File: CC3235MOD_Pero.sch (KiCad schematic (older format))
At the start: 38 parts, among them J1 USB_B_Mini, J2 JTAG/SWD, SW1 Reset, SW2 SW_DIP_x03, SW3 User IO, U1 TLV1117-33, U2 CP2102N-A01-GQFN24, U3 CC3235MODSF12MOBR

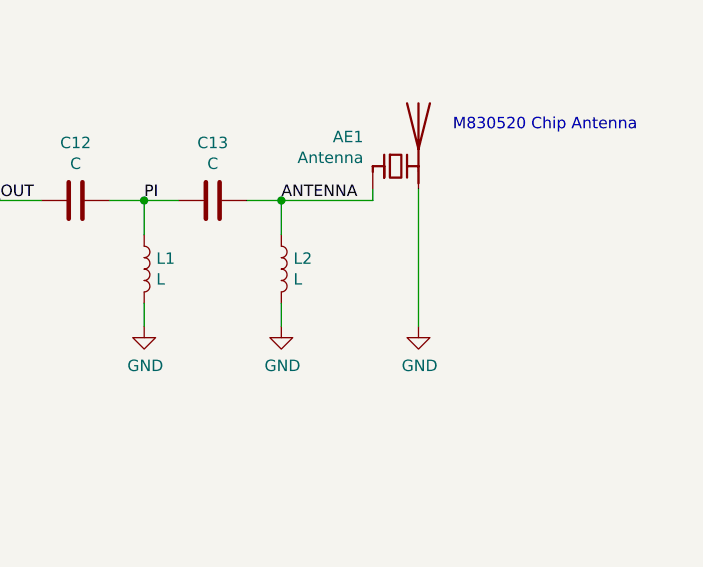
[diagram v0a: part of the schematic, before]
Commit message: fixint antenna footprint
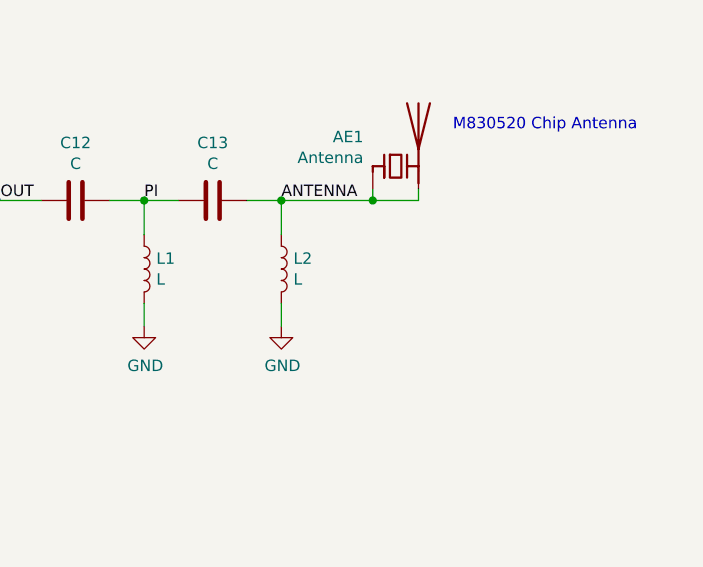
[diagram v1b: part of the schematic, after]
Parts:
- C12, C13: footprint Capacitors_SMD:C_0402 -> Capacitor_SMD:C_0603_1608Metric
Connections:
- net ANTENNA: now also AE1.2 (PCB_Trace)
- net GND: no longer AE1.2 (PCB_Trace)
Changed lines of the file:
@@
 F 0 "C12" V 12448 6700 50  0000 C CNN
 F 1 "C" V 12539 6700 50  0000 C CNN
-F 2 "Capacitors_SMD:C_0402" H 12738 6550 50  0001 C CNN
+F 2 "Capacitor_SMD:C_0603_1608Metric" H 12738 6550 50  0001 C CNN
 F 3 "~" H 12700 6700 50  0001 C CNN
 	1    12700 6700
@@
 F 0 "C13" V 13048 6700 50  0000 C CNN
 F 1 "C" V 13139 6700 50  0000 C CNN
-F 2 "Capacitors_SMD:C_0402" H 13338 6550 50  0001 C CNN
+F 2 "Capacitor_SMD:C_0603_1608Metric" H 13338 6550 50  0001 C CNN
 F 3 "~" H 13300 6700 50  0001 C CNN
 	1    13300 6700
@@
 	14000 6650 14000 6700
 Wire Wire Line
-	14200 6650 14200 7250
-$Comp
-L power:GND #PWR040
-U 1 1 5EE1CAB8
-P 14200 7250
-F 0 "#PWR040" H 14200 7000 50  0001 C CNN
-F 1 "GND" H 14205 7077 50  0000 C CNN
-F 2 "" H 14200 7250 50  0001 C CNN
-F 3 "" H 14200 7250 50  0001 C CNN
-	1    14200 7250
-	1    0    0    -1
-$EndComp
+	14200 6650 14200 6700
 NoConn ~ 11450 3250
 NoConn ~ 11450 3350
@@
 Text Label 13600 6700 0    50   ~ 0
 ANTENNA
+Wire Wire Line
+	14000 6700 14200 6700
+Connection ~ 14000 6700
 $EndSCHEMATC

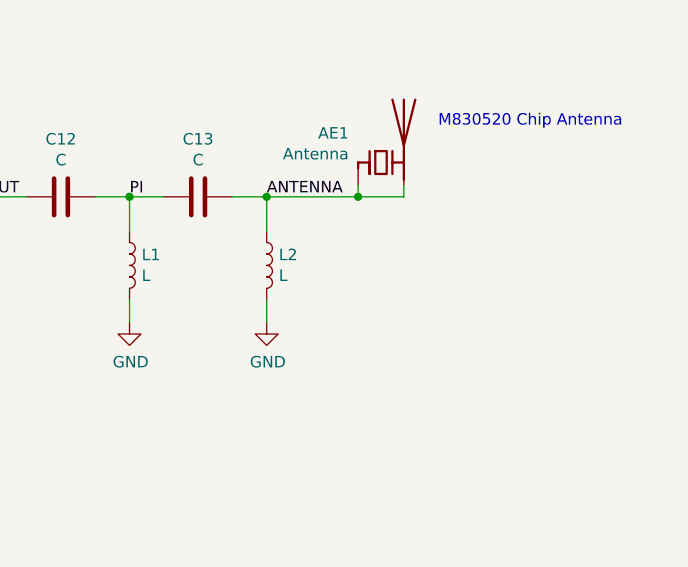
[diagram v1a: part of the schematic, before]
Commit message: antenna gnd solved
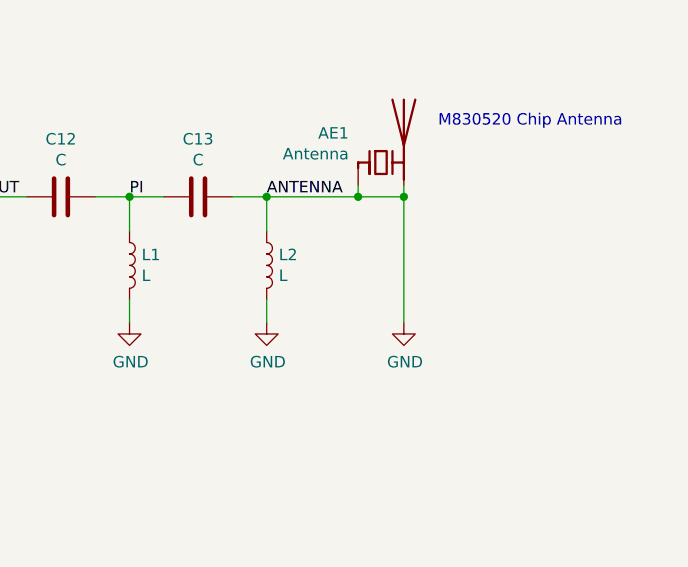
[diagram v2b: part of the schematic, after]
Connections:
- net ANTENNA is gone; now on net GND: AE1.1 (FEED), AE1.2 (PCB_Trace), C13.1, L2.1
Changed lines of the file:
@@
 	14000 6700 14200 6700
 Connection ~ 14000 6700
+$Comp
+L power:GND #PWR?
+U 1 1 5EF1A7C2
+P 14200 7250
+F 0 "#PWR?" H 14200 7000 50  0001 C CNN
+F 1 "GND" H 14205 7077 50  0000 C CNN
+F 2 "" H 14200 7250 50  0001 C CNN
+F 3 "" H 14200 7250 50  0001 C CNN
+	1    14200 7250
+	1    0    0    -1
+$EndComp
+Wire Wire Line
+	14200 7250 14200 6700
+Connection ~ 14200 6700
 $EndSCHEMATC

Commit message: fixed footprint associations AGAIN!
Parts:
- C1, C2: footprint Capacitors_SMD:C_0805 -> Capacitor_SMD:C_0805_2012Metric
- C10, C11, C3, C4, C5, C6, C7, C8, C9: footprint Capacitors_SMD:C_0603 -> Capacitor_SMD:C_0603_1608Metric
- D1: footprint TO_SOT_Packages_SMD:SOT-143 -> Package_TO_SOT_SMD:SOT-143R_Reverse; symbol CC3235MOD_Pero-rescue:SP0503BAHT-Power_Protection -> CC3235MOD_Pero-rescue:SP0503BAHT-Power_Protection-CC3235MOD_Pero-rescue
- D2, D3, D4: footprint LEDs:LED_0603 -> LED_SMD:LED_0603_1608Metric
- F1: footprint Fuse_Holders_and_Fuses:Fuse_SMD1206_Reflow -> Fuse:Fuse_1206_3216Metric
- J1: footprint Connectors_USB:USB_Micro-B_Molex-105017-0001 -> Connector_USB:USB_Micro-AB_Molex_47590-0001
- J2: footprint Pin_Headers:Pin_Header_Straight_2x05_Pitch2.54mm -> Connector_PinHeader_2.54mm:PinHeader_2x05_P2.54mm_Vertical; symbol CC3235MOD_Pero-rescue:Conn_ARM_JTAG_SWD_10-Connector -> CC3235MOD_Pero-rescue:Conn_ARM_JTAG_SWD_10-Connector-CC3235MOD_Pero-rescue
- L1, L2: footprint Inductors_SMD:L_0603 -> Inductor_SMD:L_0603_1608Metric
- R1, R2, R3, R4, R5, R6, R7, R8, R9: footprint Resistors_SMD:R_0603 -> Resistor_SMD:R_0603_1608Metric
- SW1, SW3: footprint Buttons_Switches_SMD:SW_SPST_EVQP0 -> Button_Switch_SMD:SW_SPST_EVQP0
- SW2: footprint Buttons_Switches_SMD:SW_DIP_x3_W8.61mm_Slide_LowProfile -> Button_Switch_SMD:SW_DIP_SPSTx03_Slide_6.7x9.18mm_W8.61mm_P2.54mm_LowProfile
- U1: footprint TO_SOT_Packages_SMD:SOT-223-3_TabPin2 -> Package_TO_SOT_SMD:SOT-223-3_TabPin2
- U2: footprint Housings_DFN_QFN:QFN-24-1EP_4x4mm_Pitch0.5mm -> Package_DFN_QFN:HVQFN-24-1EP_4x4mm_P0.5mm_EP2.5x2.5mm
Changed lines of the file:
@@
 $EndDescr
 $Comp
-L CC3235MOD_Pero-rescue:Conn_ARM_JTAG_SWD_10-Connector J2
+L CC3235MOD_Pero-rescue:Conn_ARM_JTAG_SWD_10-Connector-CC3235MOD_Pero-rescue J2
 U 1 1 5EC52D94
 P 6600 4450
 F 0 "J2" H 6250 5150 50  0000 R CNN
 F 1 "JTAG/SWD" H 6500 5050 50  0000 R CNN
-F 2 "Pin_Headers:Pin_Header_Straight_2x05_Pitch2.54mm" H 6650 3900 50  0001 L TNN
+F 2 "Connector_PinHeader_2.54mm:PinHeader_2x05_P2.54mm_Vertical" H 6650 3900 50  0001 L TNN
 F 3 "http://infocenter.arm.com/help/topic/com.arm.doc.faqs/attached/13634/cortex_debug_connectors.pdf" V 6250 3200 50  0001 C CNN
 	1    6600 4450
@@
 F 0 "R5" H 8300 3000 50  0000 L CNN
 F 1 "DNI(10K)" H 8050 2900 50  0000 L CNN
-F 2 "Resistors_SMD:R_0603" V 8380 2950 50  0001 C CNN
+F 2 "Resistor_SMD:R_0603_1608Metric" V 8380 2950 50  0001 C CNN
 F 3 "~" H 8450 2950 50  0001 C CNN
 	1    8450 2950
@@
 F 0 "R6" H 8820 2996 50  0000 L CNN
 F 1 "DNI" H 8820 2905 50  0000 L CNN
-F 2 "Resistors_SMD:R_0603" V 8680 2950 50  0001 C CNN
+F 2 "Resistor_SMD:R_0603_1608Metric" V 8680 2950 50  0001 C CNN
 F 3 "~" H 8750 2950 50  0001 C CNN
 	1    8750 2950
@@
 F 0 "L1" H 13053 7046 50  0000 L CNN
 F 1 "L" H 13053 6955 50  0000 L CNN
-F 2 "Inductors_SMD:L_0603" H 13000 7000 50  0001 C CNN
+F 2 "Inductor_SMD:L_0603_1608Metric" H 13000 7000 50  0001 C CNN
 F 3 "~" H 13000 7000 50  0001 C CNN
 	1    13000 7000
@@
 F 0 "L2" H 13653 7046 50  0000 L CNN
 F 1 "L" H 13653 6955 50  0000 L CNN
-F 2 "Inductors_SMD:L_0603" H 13600 7000 50  0001 C CNN
+F 2 "Inductor_SMD:L_0603_1608Metric" H 13600 7000 50  0001 C CNN
 F 3 "~" H 13600 7000 50  0001 C CNN
 	1    13600 7000
@@
 F 0 "SW1" H 8100 3735 50  0000 C CNN
 F 1 "Reset" H 8100 3644 50  0000 C CNN
-F 2 "Buttons_Switches_SMD:SW_SPST_EVQP0" H 8100 3650 50  0001 C CNN
+F 2 "Button_Switch_SMD:SW_SPST_EVQP0" H 8100 3650 50  0001 C CNN
 F 3 "" H 8100 3650 50  0001 C CNN
 	1    8100 3450
@@
 F 0 "SW2" H 8600 6217 50  0000 C CNN
 F 1 "SW_DIP_x03" H 8600 6126 50  0000 C CNN
-F 2 "Buttons_Switches_SMD:SW_DIP_x3_W8.61mm_Slide_LowProfile" H 8600 5750 50  0001 C CNN
+F 2 "Button_Switch_SMD:SW_DIP_SPSTx03_Slide_6.7x9.18mm_W8.61mm_P2.54mm_LowProfile" H 8600 5750 50  0001 C CNN
 F 3 "" H 8600 5750 50  0001 C CNN
 	1    8600 5750
@@
 F 0 "C11" H 7915 2646 50  0000 L CNN
 F 1 "100n" H 7915 2555 50  0000 L CNN
-F 2 "Capacitors_SMD:C_0603" H 7838 2450 50  0001 C CNN
+F 2 "Capacitor_SMD:C_0603_1608Metric" H 7838 2450 50  0001 C CNN
 F 3 "~" H 7800 2600 50  0001 C CNN
 	1    7800 2600
@@
 F 0 "C10" H 7515 2646 50  0000 L CNN
 F 1 "100n" H 7515 2555 50  0000 L CNN
-F 2 "Capacitors_SMD:C_0603" H 7438 2450 50  0001 C CNN
+F 2 "Capacitor_SMD:C_0603_1608Metric" H 7438 2450 50  0001 C CNN
 F 3 "~" H 7400 2600 50  0001 C CNN
 	1    7400 2600
@@
 F 0 "C9" H 7165 2646 50  0000 L CNN
 F 1 "100n" H 7165 2555 50  0000 L CNN
-F 2 "Capacitors_SMD:C_0603" H 7088 2450 50  0001 C CNN
+F 2 "Capacitor_SMD:C_0603_1608Metric" H 7088 2450 50  0001 C CNN
 F 3 "~" H 7050 2600 50  0001 C CNN
 	1    7050 2600
@@
 F 0 "C8" H 6815 2646 50  0000 L CNN
 F 1 "100n" H 6815 2555 50  0000 L CNN
-F 2 "Capacitors_SMD:C_0603" H 6738 2450 50  0001 C CNN
+F 2 "Capacitor_SMD:C_0603_1608Metric" H 6738 2450 50  0001 C CNN
 F 3 "~" H 6700 2600 50  0001 C CNN
 	1    6700 2600
@@
 F 0 "C7" H 6465 2646 50  0000 L CNN
 F 1 "100n" H 6465 2555 50  0000 L CNN
-F 2 "Capacitors_SMD:C_0603" H 6388 2450 50  0001 C CNN
+F 2 "Capacitor_SMD:C_0603_1608Metric" H 6388 2450 50  0001 C CNN
 F 3 "~" H 6350 2600 50  0001 C CNN
 	1    6350 2600
@@
 F 0 "SW3" V 12504 3448 50  0000 L CNN
 F 1 "User IO" V 12595 3448 50  0000 L CNN
-F 2 "Buttons_Switches_SMD:SW_SPST_EVQP0" H 12550 3500 50  0001 C CNN
+F 2 "Button_Switch_SMD:SW_SPST_EVQP0" H 12550 3500 50  0001 C CNN
 F 3 "" H 12550 3500 50  0001 C CNN
 	1    12550 3300
@@
 F 0 "D2" V 12250 5150 50  0000 R CNN
 F 1 "LED_ALT" V 12097 4932 50  0001 R CNN
-F 2 "LEDs:LED_0603" H 12150 5050 50  0001 C CNN
+F 2 "LED_SMD:LED_0603_1608Metric" H 12150 5050 50  0001 C CNN
 F 3 "~" H 12150 5050 50  0001 C CNN
 	1    12150 5050
@@
 F 0 "R7" H 12000 4750 50  0000 L CNN
 F 1 "100" H 11950 4650 50  0001 L CNN
-F 2 "Resistors_SMD:R_0603" V 12080 4700 50  0001 C CNN
+F 2 "Resistor_SMD:R_0603_1608Metric" V 12080 4700 50  0001 C CNN
 F 3 "~" H 12150 4700 50  0001 C CNN
 	1    12150 4700
@@
 F 0 "D3" V 12450 5150 50  0000 R CNN
 F 1 "LED_ALT" V 12297 4932 50  0001 R CNN
-F 2 "LEDs:LED_0603" H 12350 5050 50  0001 C CNN
+F 2 "LED_SMD:LED_0603_1608Metric" H 12350 5050 50  0001 C CNN
 F 3 "~" H 12350 5050 50  0001 C CNN
 	1    12350 5050
@@
 F 0 "R8" H 12200 4750 50  0000 L CNN
 F 1 "100" H 12200 4650 50  0001 L CNN
-F 2 "Resistors_SMD:R_0603" V 12280 4700 50  0001 C CNN
+F 2 "Resistor_SMD:R_0603_1608Metric" V 12280 4700 50  0001 C CNN
 F 3 "~" H 12350 4700 50  0001 C CNN
 	1    12350 4700
@@
 F 0 "D4" V 12650 5150 50  0000 R CNN
 F 1 "LED_ALT" V 12497 4932 50  0001 R CNN
-F 2 "LEDs:LED_0603" H 12550 5050 50  0001 C CNN
+F 2 "LED_SMD:LED_0603_1608Metric" H 12550 5050 50  0001 C CNN
 F 3 "~" H 12550 5050 50  0001 C CNN
 	1    12550 5050
@@
 F 0 "R9" H 12400 4750 50  0000 L CNN
 F 1 "100" H 12400 4650 50  0001 L CNN
-F 2 "Resistors_SMD:R_0603" V 12480 4700 50  0001 C CNN
+F 2 "Resistor_SMD:R_0603_1608Metric" V 12480 4700 50  0001 C CNN
 F 3 "~" H 12550 4700 50  0001 C CNN
 	1    12550 4700
@@
 F 0 "U2" H 3850 9900 50  0000 C CNN
 F 1 "CP2102N-A01-GQFN24" H 4850 8250 50  0000 C CNN
-F 2 "Housings_DFN_QFN:QFN-24-1EP_4x4mm_Pitch0.5mm" H 4700 8300 50  0001 L CNN
+F 2 "Package_DFN_QFN:HVQFN-24-1EP_4x4mm_P0.5mm_EP2.5x2.5mm" H 4700 8300 50  0001 L CNN
 F 3 "http://www.silabs.com/support%20documents/technicaldocs/cp2102n-datasheet.pdf" H 4300 8050 50  0001 C CNN
 	1    4250 9100
@@
 F 0 "R3" H 3520 8046 50  0000 L CNN
 F 1 "1K" H 3520 7955 50  0000 L CNN
-F 2 "Resistors_SMD:R_0603" V 3380 8000 50  0001 C CNN
+F 2 "Resistor_SMD:R_0603_1608Metric" V 3380 8000 50  0001 C CNN
 F 3 "~" H 3450 8000 50  0001 C CNN
 	1    3450 8000
@@
 F 0 "C2" H 2200 9350 50  0000 L CNN
 F 1 "4.7u" H 2100 9250 50  0000 L CNN
-F 2 "Capacitors_SMD:C_0805" H 2438 9150 50  0001 C CNN
+F 2 "Capacitor_SMD:C_0805_2012Metric" H 2438 9150 50  0001 C CNN
 F 3 "~" H 2400 9300 50  0001 C CNN
 	1    2400 9300
@@
 F 0 "R2" H 3320 9846 50  0000 L CNN
 F 1 "47.5K" H 3320 9755 50  0000 L CNN
-F 2 "Resistors_SMD:R_0603" V 3180 9800 50  0001 C CNN
+F 2 "Resistor_SMD:R_0603_1608Metric" V 3180 9800 50  0001 C CNN
 F 3 "~" H 3250 9800 50  0001 C CNN
 	1    3250 9800
@@
 F 0 "R1" H 3320 9296 50  0000 L CNN
 F 1 "22.1K" H 3320 9205 50  0000 L CNN
-F 2 "Resistors_SMD:R_0603" V 3180 9250 50  0001 C CNN
+F 2 "Resistor_SMD:R_0603_1608Metric" V 3180 9250 50  0001 C CNN
 F 3 "~" H 3250 9250 50  0001 C CNN
 	1    3250 9250
@@
 D+
 $Comp
-L CC3235MOD_Pero-rescue:SP0503BAHT-Power_Protection D1
+L CC3235MOD_Pero-rescue:SP0503BAHT-Power_Protection-CC3235MOD_Pero-rescue D1
 U 1 1 5ECF8AC1
 P 1800 9850
 F 0 "D1" H 2005 9896 50  0000 L CNN
 F 1 "SP0503BAHT" H 1850 9700 50  0000 L CNN
-F 2 "TO_SOT_Packages_SMD:SOT-143" H 2025 9800 50  0001 L CNN
+F 2 "Package_TO_SOT_SMD:SOT-143R_Reverse" H 2025 9800 50  0001 L CNN
 F 3 "http://www.littelfuse.com/~/media/files/littelfuse/technical%20resources/documents/data%20sheets/sp05xxba.pdf" H 1925 9975 50  0001 C CNN
 	1    1800 9850
@@
 F 0 "C5" H 4615 7846 50  0000 L CNN
 F 1 "100n" H 4615 7755 50  0000 L CNN
-F 2 "Capacitors_SMD:C_0603" H 4538 7650 50  0001 C CNN
+F 2 "Capacitor_SMD:C_0603_1608Metric" H 4538 7650 50  0001 C CNN
 F 3 "~" H 4500 7800 50  0001 C CNN
 	1    4500 7800
@@
 F 0 "C6" H 5015 7846 50  0000 L CNN
 F 1 "100n" H 5015 7755 50  0000 L CNN
-F 2 "Capacitors_SMD:C_0603" H 4938 7650 50  0001 C CNN
+F 2 "Capacitor_SMD:C_0603_1608Metric" H 4938 7650 50  0001 C CNN
 F 3 "~" H 4900 7800 50  0001 C CNN
 	1    4900 7800
@@
 F 0 "J1" H 1105 9967 50  0000 C CNN
 F 1 "USB_B_Mini" H 1105 9876 50  0000 C CNN
-F 2 "Connectors_USB:USB_Micro-B_Molex-105017-0001" H 1200 9450 50  0001 C CNN
+F 2 "Connector_USB:USB_Micro-AB_Molex_47590-0001" H 1200 9450 50  0001 C CNN
 F 3 "~" H 1200 9450 50  0001 C CNN
 	1    1050 9500
@@
 F 0 "C4" H 2765 9346 50  0000 L CNN
 F 1 "100n" H 2765 9255 50  0000 L CNN
-F 2 "Capacitors_SMD:C_0603" H 2688 9150 50  0001 C CNN
+F 2 "Capacitor_SMD:C_0603_1608Metric" H 2688 9150 50  0001 C CNN
 F 3 "~" H 2650 9300 50  0001 C CNN
 	1    2650 9300
@@
 F 0 "F1" V 1803 9100 50  0000 C CNN
 F 1 "Fuse" V 1894 9100 50  0000 C CNN
-F 2 "Fuse_Holders_and_Fuses:Fuse_SMD1206_Reflow" V 1930 9100 50  0001 C CNN
+F 2 "Fuse:Fuse_1206_3216Metric" V 1930 9100 50  0001 C CNN
 F 3 "~" H 2000 9100 50  0001 C CNN
 	1    2000 9100
@@
 F 0 "U1" H 2200 6692 50  0000 C CNN
 F 1 "TLV1117-33" H 2200 6601 50  0000 C CNN
-F 2 "TO_SOT_Packages_SMD:SOT-223-3_TabPin2" H 2200 6450 50  0001 C CNN
+F 2 "Package_TO_SOT_SMD:SOT-223-3_TabPin2" H 2200 6450 50  0001 C CNN
 F 3 "http://www.ti.com/lit/ds/symlink/tlv1117.pdf" H 2200 6450 50  0001 C CNN
 	1    2200 6450
@@
 F 0 "C3" H 2765 6796 50  0000 L CNN
 F 1 "100n" H 2765 6705 50  0000 L CNN
-F 2 "Capacitors_SMD:C_0603" H 2688 6600 50  0001 C CNN
+F 2 "Capacitor_SMD:C_0603_1608Metric" H 2688 6600 50  0001 C CNN
 F 3 "~" H 2650 6750 50  0001 C CNN
 	1    2650 6750
@@
 F 0 "C1" H 1815 6796 50  0000 L CNN
 F 1 "4.7u" H 1815 6705 50  0000 L CNN
-F 2 "Capacitors_SMD:C_0805" H 1738 6600 50  0001 C CNN
+F 2 "Capacitor_SMD:C_0805_2012Metric" H 1738 6600 50  0001 C CNN
 F 3 "~" H 1700 6750 50  0001 C CNN
 	1    1700 6750
@@
 F 0 "R4" H 8020 5396 50  0000 L CNN
 F 1 "10k" H 8020 5305 50  0000 L CNN
-F 2 "Resistors_SMD:R_0603" V 7880 5350 50  0001 C CNN
+F 2 "Resistor_SMD:R_0603_1608Metric" V 7880 5350 50  0001 C CNN
 F 3 "~" H 7950 5350 50  0001 C CNN
 	1    7950 5350
@@
 Connection ~ 14000 6700
 $Comp
-L power:GND #PWR?
+L power:GND #PWR0102
 U 1 1 5EF1A7C2
 P 14200 7250
-F 0 "#PWR?" H 14200 7000 50  0001 C CNN
+F 0 "#PWR0102" H 14200 7000 50  0001 C CNN
 F 1 "GND" H 14205 7077 50  0000 C CNN
 F 2 "" H 14200 7250 50  0001 C CNN
